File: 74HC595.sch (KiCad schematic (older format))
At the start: 10 parts, among them P2 CONN_02X08, U1 74HC595

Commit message: расставлено по сетке, исправлены ошибки
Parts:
- added C1: C, Capacitors_SMD:C_0805_HandSoldering, symbol C
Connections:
- net GND: now also C1.1
- net VCC: now also C1.2
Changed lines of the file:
@@
 LIBS:contrib
 LIBS:valves
+LIBS:74HC595x4-cache
 EELAYER 25 0
 EELAYER END
@@
 AR Path="/57D7673A/57D72B62" Ref="U3"  Part="1"
 AR Path="/57D76743/57D72B62" Ref="U4"  Part="1"
-F 0 "U4" H 5900 3850 50  0000 C CNN
+F 0 "U3" H 5900 3850 50  0000 C CNN
 F 1 "74HC595" H 5750 2650 50  0000 C CNN
 F 2 "SMD_Packages:SO-16-N" H 5750 3250 50  0001 C CNN
@@
 AR Path="/57D7673A/57D72B69" Ref="R17"  Part="1"
 AR Path="/57D76743/57D72B69" Ref="R25"  Part="1"
-F 0 "R25" V 7030 2800 50  0000 C CNN
+F 0 "R17" V 7030 2800 50  0000 C CNN
 F 1 "R" V 6950 2800 50  0000 C CNN
 F 2 "Resistors_SMD:R_0805_HandSoldering" V 6880 2800 50  0001 C CNN
@@
 AR Path="/57D7673A/57D72B70" Ref="R21"  Part="1"
 AR Path="/57D76743/57D72B70" Ref="R29"  Part="1"
-F 0 "R29" V 7480 2900 50  0000 C CNN
+F 0 "R21" V 7480 2900 50  0000 C CNN
 F 1 "R" V 7400 2900 50  0000 C CNN
 F 2 "Resistors_SMD:R_0805_HandSoldering" V 7330 2900 50  0001 C CNN
@@
 AR Path="/57D7673A/57D72B77" Ref="P4"  Part="1"
 AR Path="/57D76743/57D72B77" Ref="P5"  Part="1"
-F 0 "P5" H 8250 3600 50  0000 C CNN
+F 0 "P4" H 8250 3600 50  0000 C CNN
 F 1 "CONN_02X08" V 8250 3150 50  0000 C CNN
 F 2 "Pin_Headers:Pin_Header_Straight_2x08" H 8250 1950 50  0001 C CNN
@@
 AR Path="/57D7673A/57D72B7F" Ref="R18"  Part="1"
 AR Path="/57D76743/57D72B7F" Ref="R26"  Part="1"
-F 0 "R26" V 7030 3000 50  0000 C CNN
+F 0 "R18" V 7030 3000 50  0000 C CNN
 F 1 "R" V 6950 3000 50  0000 C CNN
 F 2 "Resistors_SMD:R_0805_HandSoldering" V 6880 3000 50  0001 C CNN
@@
 AR Path="/57D7673A/57D72B86" Ref="R22"  Part="1"
 AR Path="/57D76743/57D72B86" Ref="R30"  Part="1"
-F 0 "R30" V 7480 3100 50  0000 C CNN
+F 0 "R22" V 7480 3100 50  0000 C CNN
 F 1 "R" V 7400 3100 50  0000 C CNN
 F 2 "Resistors_SMD:R_0805_HandSoldering" V 7330 3100 50  0001 C CNN
@@
 AR Path="/57D7673A/57D72B8D" Ref="R19"  Part="1"
 AR Path="/57D76743/57D72B8D" Ref="R27"  Part="1"
-F 0 "R27" V 7030 3200 50  0000 C CNN
+F 0 "R19" V 7030 3200 50  0000 C CNN
 F 1 "R" V 6950 3200 50  0000 C CNN
 F 2 "Resistors_SMD:R_0805_HandSoldering" V 6880 3200 50  0001 C CNN
@@
 AR Path="/57D7673A/57D72B94" Ref="R23"  Part="1"
 AR Path="/57D76743/57D72B94" Ref="R31"  Part="1"
-F 0 "R31" V 7480 3300 50  0000 C CNN
+F 0 "R23" V 7480 3300 50  0000 C CNN
 F 1 "R" V 7400 3300 50  0000 C CNN
 F 2 "Resistors_SMD:R_0805_HandSoldering" V 7330 3300 50  0001 C CNN
@@
 AR Path="/57D7673A/57D72B9B" Ref="R20"  Part="1"
 AR Path="/57D76743/57D72B9B" Ref="R28"  Part="1"
-F 0 "R28" V 7030 3400 50  0000 C CNN
+F 0 "R20" V 7030 3400 50  0000 C CNN
 F 1 "R" V 6950 3400 50  0000 C CNN
 F 2 "Resistors_SMD:R_0805_HandSoldering" V 6880 3400 50  0001 C CNN
@@
 AR Path="/57D7673A/57D72BA2" Ref="R24"  Part="1"
 AR Path="/57D76743/57D72BA2" Ref="R32"  Part="1"
-F 0 "R32" V 7480 3500 50  0000 C CNN
+F 0 "R24" V 7480 3500 50  0000 C CNN
 F 1 "R" V 7400 3500 50  0000 C CNN
 F 2 "Resistors_SMD:R_0805_HandSoldering" V 7330 3500 50  0001 C CNN
@@
 	8500 2800 8900 2800
 Wire Wire Line
-	8900 2800 8900 4500
+	8900 2300 8900 4500
 Wire Wire Line
 	8900 2900 8500 2900
@@
 	8900 4500 4300 4500
 Connection ~ 4300 4500
+$Comp
+L C C1
+U 1 1 580CA56D
+P 5750 2300
+AR Path="/57D72395/580CA56D" Ref="C1"  Part="1"
+AR Path="/57D75B94/580CA56D" Ref="C2"  Part="1"
+AR Path="/57D7673A/580CA56D" Ref="C3"  Part="1"
+AR Path="/57D76743/580CA56D" Ref="C4"  Part="1"
+F 0 "C3" H 5775 2400 50  0000 L CNN
+F 1 "C" H 5775 2200 50  0000 L CNN
+F 2 "Capacitors_SMD:C_0805_HandSoldering" H 5788 2150 50  0001 C CNN
+F 3 "" H 5750 2300 50  0000 C CNN
+	1    5750 2300
+	0    1    1    0
+$EndComp
+Wire Wire Line
+	5600 2300 4300 2300
+Connection ~ 4300 2300
+Wire Wire Line
+	5900 2300 8900 2300
+Connection ~ 8900 2800
 $EndSCHEMATC

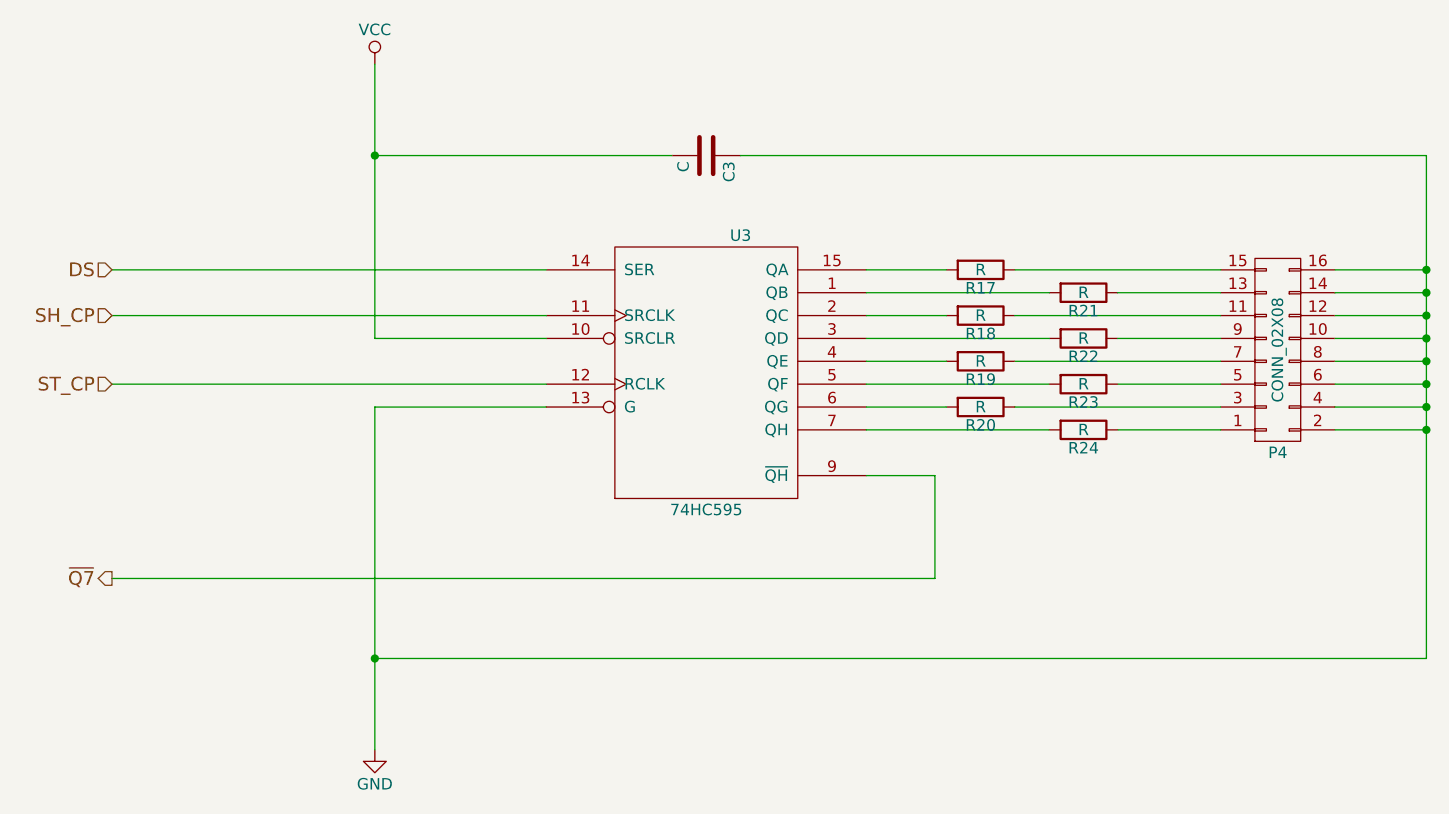
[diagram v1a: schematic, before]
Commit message: изменен входной разъем
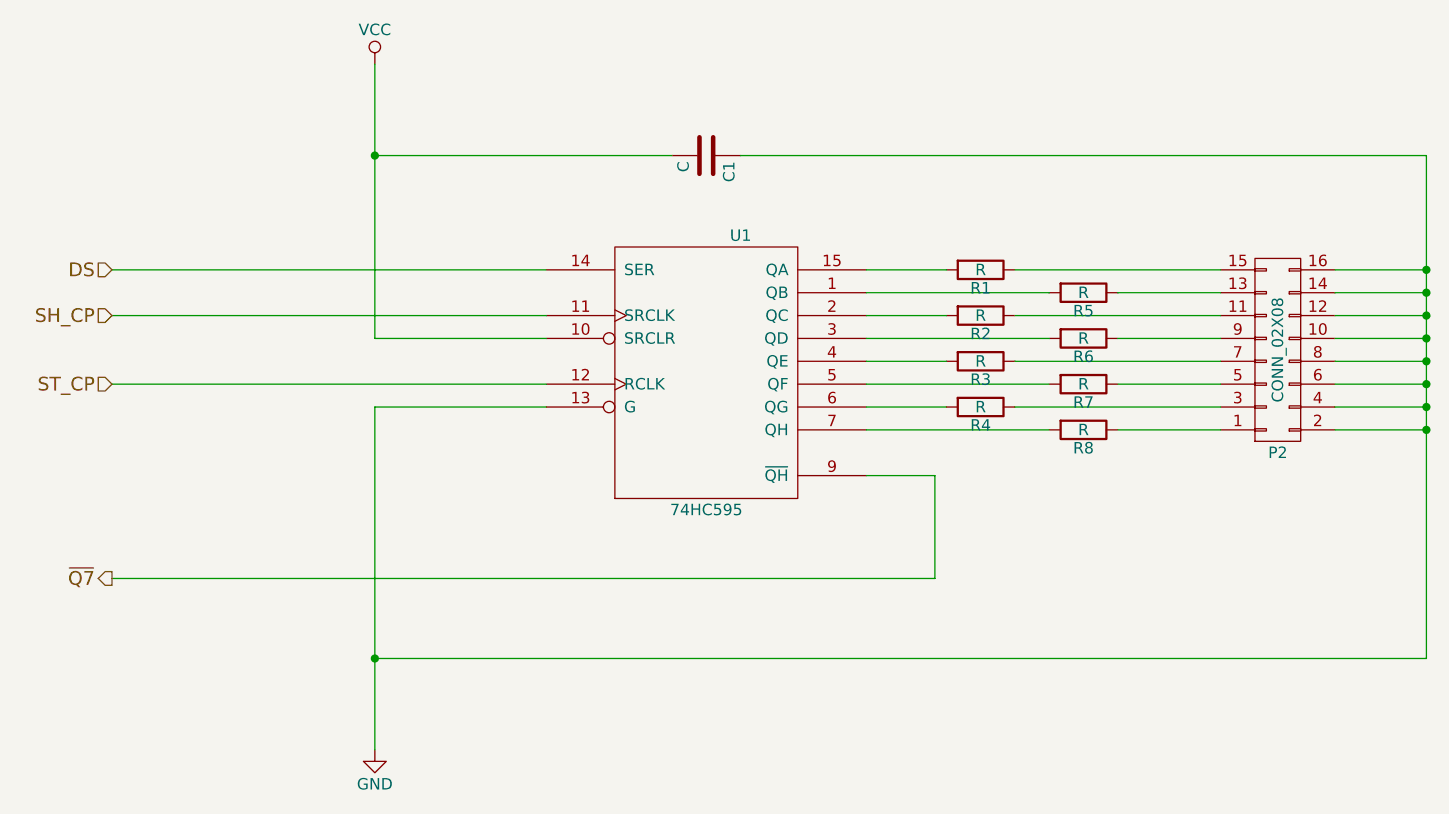
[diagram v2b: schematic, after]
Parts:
- P2: footprint Pin_Headers:Pin_Header_Straight_2x08 -> Connect:IDC_Header_Straight_16pins
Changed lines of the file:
@@
 AR Path="/57D7673A/57D72B62" Ref="U3"  Part="1"
 AR Path="/57D76743/57D72B62" Ref="U4"  Part="1"
-F 0 "U3" H 5900 3850 50  0000 C CNN
+F 0 "U1" H 5900 3850 50  0000 C CNN
 F 1 "74HC595" H 5750 2650 50  0000 C CNN
 F 2 "SMD_Packages:SO-16-N" H 5750 3250 50  0001 C CNN
@@
 AR Path="/57D7673A/57D72B69" Ref="R17"  Part="1"
 AR Path="/57D76743/57D72B69" Ref="R25"  Part="1"
-F 0 "R17" V 7030 2800 50  0000 C CNN
+F 0 "R1" V 7030 2800 50  0000 C CNN
 F 1 "R" V 6950 2800 50  0000 C CNN
 F 2 "Resistors_SMD:R_0805_HandSoldering" V 6880 2800 50  0001 C CNN
@@
 AR Path="/57D7673A/57D72B70" Ref="R21"  Part="1"
 AR Path="/57D76743/57D72B70" Ref="R29"  Part="1"
-F 0 "R21" V 7480 2900 50  0000 C CNN
+F 0 "R5" V 7480 2900 50  0000 C CNN
 F 1 "R" V 7400 2900 50  0000 C CNN
 F 2 "Resistors_SMD:R_0805_HandSoldering" V 7330 2900 50  0001 C CNN
@@
 AR Path="/57D7673A/57D72B77" Ref="P4"  Part="1"
 AR Path="/57D76743/57D72B77" Ref="P5"  Part="1"
-F 0 "P4" H 8250 3600 50  0000 C CNN
+F 0 "P2" H 8250 3600 50  0000 C CNN
 F 1 "CONN_02X08" V 8250 3150 50  0000 C CNN
-F 2 "Pin_Headers:Pin_Header_Straight_2x08" H 8250 1950 50  0001 C CNN
+F 2 "Connect:IDC_Header_Straight_16pins" H 8250 1950 50  0001 C CNN
 F 3 "" H 8250 1950 50  0000 C CNN
 	1    8250 3150
@@
 AR Path="/57D7673A/57D72B7F" Ref="R18"  Part="1"
 AR Path="/57D76743/57D72B7F" Ref="R26"  Part="1"
-F 0 "R18" V 7030 3000 50  0000 C CNN
+F 0 "R2" V 7030 3000 50  0000 C CNN
 F 1 "R" V 6950 3000 50  0000 C CNN
 F 2 "Resistors_SMD:R_0805_HandSoldering" V 6880 3000 50  0001 C CNN
@@
 AR Path="/57D7673A/57D72B86" Ref="R22"  Part="1"
 AR Path="/57D76743/57D72B86" Ref="R30"  Part="1"
-F 0 "R22" V 7480 3100 50  0000 C CNN
+F 0 "R6" V 7480 3100 50  0000 C CNN
 F 1 "R" V 7400 3100 50  0000 C CNN
 F 2 "Resistors_SMD:R_0805_HandSoldering" V 7330 3100 50  0001 C CNN
@@
 AR Path="/57D7673A/57D72B8D" Ref="R19"  Part="1"
 AR Path="/57D76743/57D72B8D" Ref="R27"  Part="1"
-F 0 "R19" V 7030 3200 50  0000 C CNN
+F 0 "R3" V 7030 3200 50  0000 C CNN
 F 1 "R" V 6950 3200 50  0000 C CNN
 F 2 "Resistors_SMD:R_0805_HandSoldering" V 6880 3200 50  0001 C CNN
@@
 AR Path="/57D7673A/57D72B94" Ref="R23"  Part="1"
 AR Path="/57D76743/57D72B94" Ref="R31"  Part="1"
-F 0 "R23" V 7480 3300 50  0000 C CNN
+F 0 "R7" V 7480 3300 50  0000 C CNN
 F 1 "R" V 7400 3300 50  0000 C CNN
 F 2 "Resistors_SMD:R_0805_HandSoldering" V 7330 3300 50  0001 C CNN
@@
 AR Path="/57D7673A/57D72B9B" Ref="R20"  Part="1"
 AR Path="/57D76743/57D72B9B" Ref="R28"  Part="1"
-F 0 "R20" V 7030 3400 50  0000 C CNN
+F 0 "R4" V 7030 3400 50  0000 C CNN
 F 1 "R" V 6950 3400 50  0000 C CNN
 F 2 "Resistors_SMD:R_0805_HandSoldering" V 6880 3400 50  0001 C CNN
@@
 AR Path="/57D7673A/57D72BA2" Ref="R24"  Part="1"
 AR Path="/57D76743/57D72BA2" Ref="R32"  Part="1"
-F 0 "R24" V 7480 3500 50  0000 C CNN
+F 0 "R8" V 7480 3500 50  0000 C CNN
 F 1 "R" V 7400 3500 50  0000 C CNN
 F 2 "Resistors_SMD:R_0805_HandSoldering" V 7330 3500 50  0001 C CNN
@@
 AR Path="/57D7673A/580CA56D" Ref="C3"  Part="1"
 AR Path="/57D76743/580CA56D" Ref="C4"  Part="1"
-F 0 "C3" H 5775 2400 50  0000 L CNN
+F 0 "C1" H 5775 2400 50  0000 L CNN
 F 1 "C" H 5775 2200 50  0000 L CNN
 F 2 "Capacitors_SMD:C_0805_HandSoldering" H 5788 2150 50  0001 C CNN
